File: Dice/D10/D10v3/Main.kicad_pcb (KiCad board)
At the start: 2 copper layers, 67.4 x 42.1 mm, 65 parts, among them J1 Conn_01x14, J2 Conn_01x04, J3 Conn_01x02, J4 DNP, P5 COILA, P6 COILB, U1 N52810_QFN32, U2 KXTJ3-1057, U3 PJ75AL50SA, U4 ME6215, U5 MCP73832T-2ACI/OT, U6 MT9700, U7 SN74LVC1G08, U8 TMR1366, Y1 32MHz 40ppm

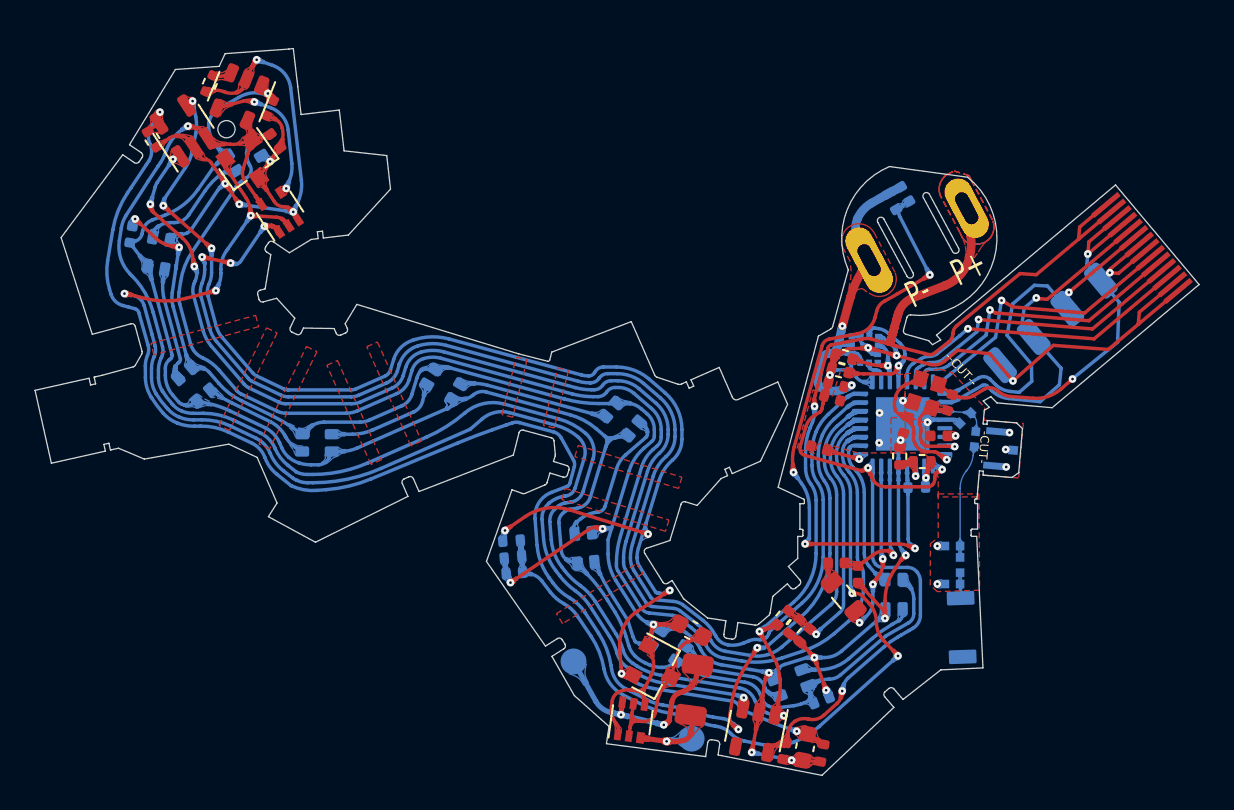
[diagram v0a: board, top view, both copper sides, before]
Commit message: New Version of All boards! Better Sticky tape shapes, tweaks to board outline, changed C19 footprint, revert coil pads to through holes. Also updated to Kicad 7.
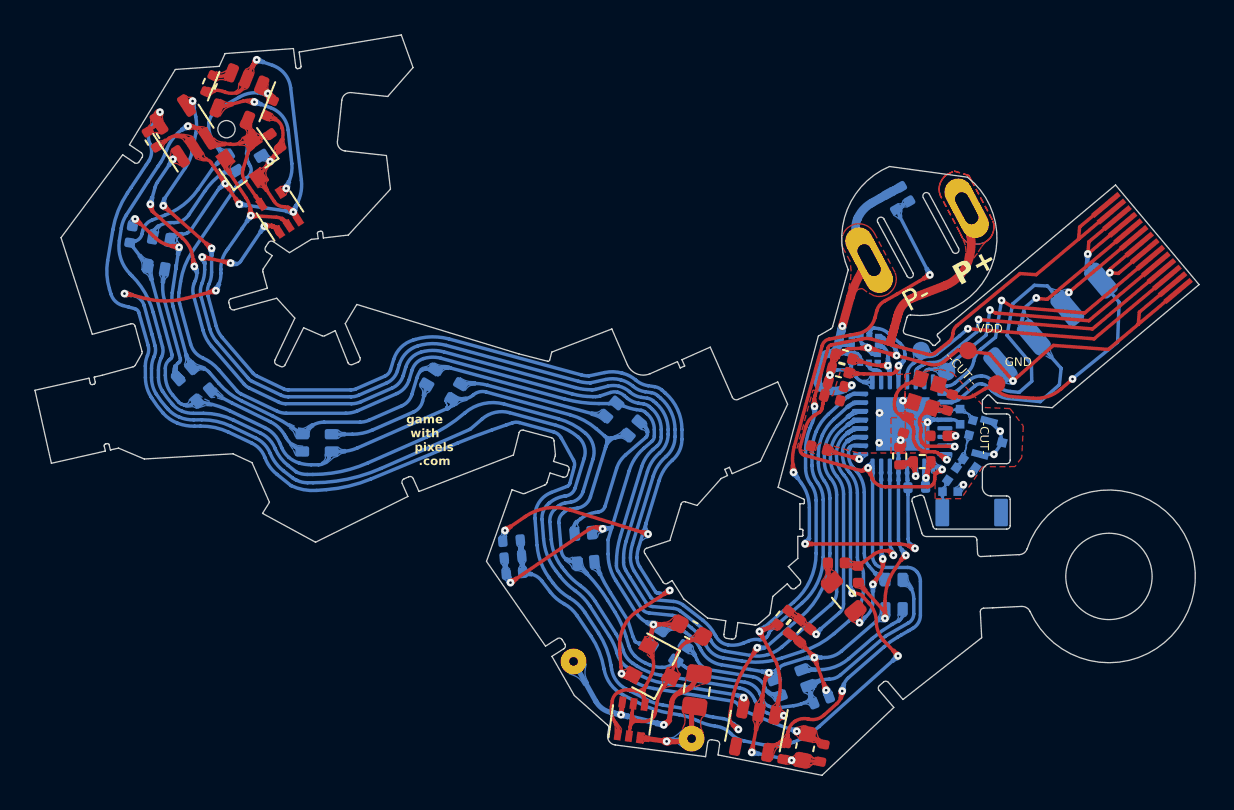
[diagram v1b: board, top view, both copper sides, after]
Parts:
- added W1: RXI, Pixels-dice:TEST_PIN, B.Cu at (153.6, 107.8)
- added W19: GND, Pixels-dice:TEST_PIN, F.Cu at (156.5, 108.5)
- added W2: TXO, Pixels-dice:TEST_PIN, B.Cu at (152.1, 106.6)
- added W25: VDD, Pixels-dice:TEST_PIN, F.Cu at (154.8, 106.6)
- C12: value 0.5pF 10V 5% C0G -> DNP
- C19: value 33nF 50V 5% NP0 -> 12nF 50V 5% NP0; footprint Capacitor_SMD:C_1206_3216Metric -> Capacitor_SMD:C_0805_2012Metric
- L3: value 1.8nH 5% -> 0 Ohm
- P5, P6: footprint TestPoint:TestPoint_Pad_D1.5mm -> TestPoint:TestPoint_THTPad_D1.5mm_Drill0.7mm
- moved C11 5.35 mm to (153.8, 114.7), turned to 0 degrees
- moved L3 5.29 mm to (153.9, 113.7), turned to -125 degrees
- moved AE1 5.07 mm to (153.3, 116.0), turned to 90 degrees
- moved C12 4.90 mm to (154.9, 113.1), turned to -35 degrees
- moved J4 0.88 mm to (155.8, 111.6), turned to -105 degrees
- moved L5 0.71 mm to (155.0, 111.0), turned to -105 degrees
- moved C8 0.31 mm to (154.3, 110.4), turned to -90 degrees
- moved C19 0.15 mm to (139.1, 126.2)
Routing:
- net /ANT_50: track 6.59 -> 2.08 mm
- net GND: track 218.1 -> 219.5 mm, vias 32 -> 31
- net /ANT_NRF: track 2.67 -> 1.76 mm
- net Net-(C19-Pad2): track 12.1 -> 11.3 mm
- added copper zone on B.Cu, net /BATT_NTC
- added copper zone on F.Cu, net Net-(C19-Pad2)
- added copper zone on B.Cu, net RXI
- added copper zone on B.Cu, net SWDCLK
- added copper zone on B.Cu, net SWDIO
- added copper zone on B.Cu, net TXO
- removed copper zone on F.Cu, net (none)
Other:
- board size 67.4 x 42.1 mm -> 67.4 x 42.9 mm
- board text added: "PIXELS D10 V3 PCB"
- board text added: "SYSTEMIC GAMES"
- board text added: "game with pixels .com"
- board text removed: "PIXELS D10 V3 PCB SYSTEMIC GAMES"

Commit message: Updated all boards based on Wang Qing's feedback. Generated renders of all boards. Updated LCC to Kicad 7.
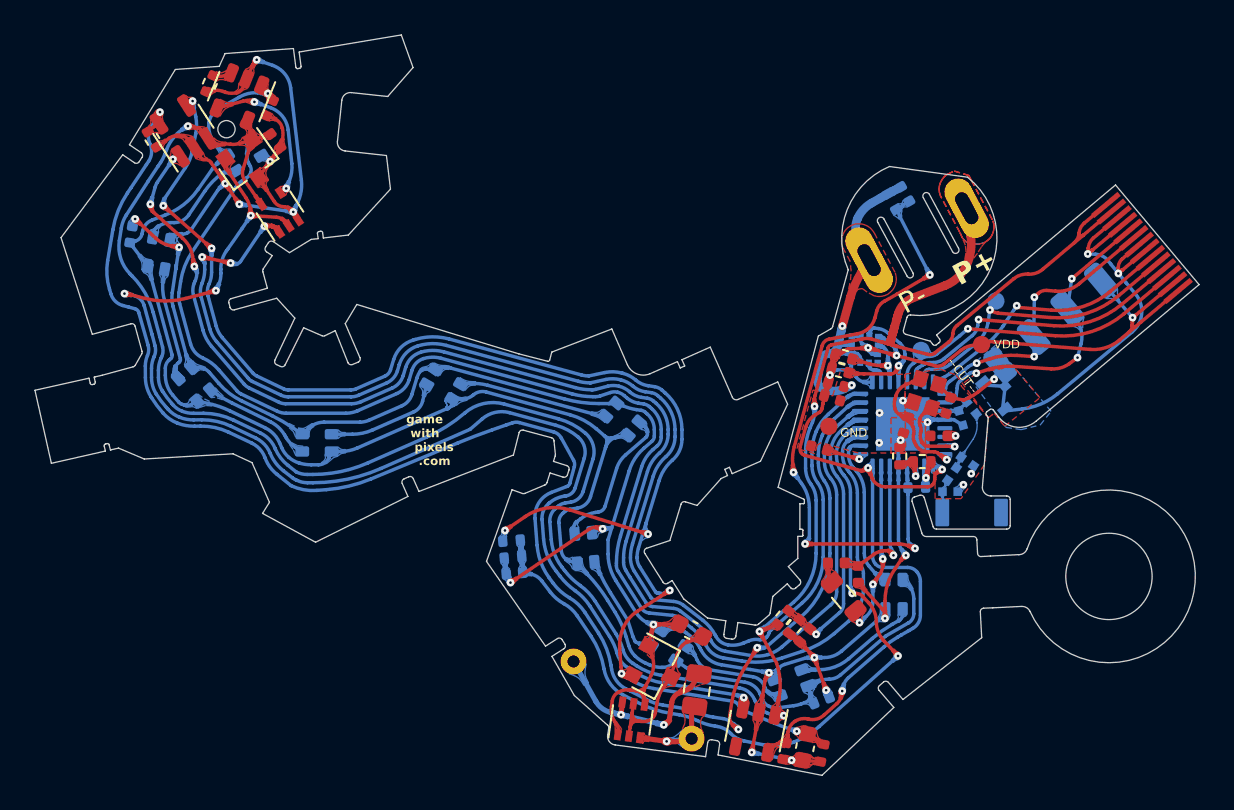
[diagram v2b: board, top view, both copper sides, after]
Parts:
- moved W19 10.0 mm to (146.8, 111.0)
- moved W1 5.00 mm to (156.4, 103.7)
- moved J4 2.33 mm to (156.2, 109.3), turned to -50 degrees
- moved L5 1.14 mm to (155.0, 109.9), turned to -52 degrees
- moved W25 0.85 mm to (155.6, 106.2)
- moved C5 0.19 mm to (153.7, 109.8)
- moved C12 0.16 mm to (154.8, 113.0)
- moved C8 0.09 mm to (154.4, 110.5), turned to -74 degrees
- turned J2 to -140 degrees
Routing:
- net SWDCLK: track 20.9 -> 16.5 mm, vias 1 -> 3
- net GND: track 219.5 -> 222.3 mm, vias 31 -> 29
- net SWDIO: track 20.6 -> 18.1 mm, vias 1 -> 3
- net VDD: track 75.2 -> 77.0 mm
- net RESET: track 17.0 -> 15.4 mm
- net /ANT_50: track 2.08 -> 3.43 mm
- net Net-(C5-Pad2): track 5.43 -> 4.82 mm
- removed copper zone on B.Cu, net RXI
- removed copper zone on B.Cu, net SWDCLK
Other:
- outline, holes or cut-outs redrawn
- board text removed: "-CUT-"
